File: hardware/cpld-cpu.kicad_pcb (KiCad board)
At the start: 4 copper layers, 264.2 x 190.5 mm, 386 parts, among them J1 Acc, J10 Page, J11 PC_H, J12 Conn_02x16_Odd_Even, J13 Page, J14 Conn_02x16_Odd_Even, J2 X, J3 IR, J4 AXM, J5 Dec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

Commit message: More routing
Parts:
- moved R133 167.5 mm to (281.4, 246.1)
- moved R136 167.5 mm to (281.4, 253.7)
- moved R134 167.5 mm to (281.4, 248.7)
- moved R135 167.5 mm to (281.4, 251.2)
- moved R123 155.6 mm to (281.4, 240.8)
- moved R124 155.6 mm to (281.4, 243.3)
- moved J14 150.6 mm to (266.7, 248.9)
- moved R108 66.0 mm to (190.5, 147.3), turned to 270 degrees
- moved R107 62.7 mm to (188.0, 147.3), turned to 270 degrees
- moved R109 62.5 mm to (185.4, 147.3), turned to 270 degrees
- moved R110 61.4 mm to (182.9, 147.3), turned to 270 degrees
- moved R111 60.6 mm to (180.3, 147.3), turned to 270 degrees
- moved R112 59.9 mm to (177.8, 147.3), turned to 270 degrees
- moved R113 59.5 mm to (175.3, 147.3), turned to 270 degrees
- moved R114 59.3 mm to (172.7, 147.3), turned to 270 degrees
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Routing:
- net /ADDR12: track 0.00 -> 156.2 mm, vias 0 -> 2
- net /IR4: track 17.9 -> 158.7 mm, vias 0 -> 2
- net /ADDR8: track 0.00 -> 134.8 mm, vias 0 -> 3
- net /ADDR9: track 0.00 -> 133.0 mm, vias 0 -> 3
- net /ADDR11: track 0.00 -> 132.8 mm, vias 0 -> 3
- net /ADDR10: track 0.00 -> 132.6 mm, vias 0 -> 3
- net /IR3: track 22.6 -> 151.0 mm, vias 0 -> 2
- net /IR2: track 22.8 -> 148.7 mm, vias 0 -> 2
- net /IR1: track 22.9 -> 145.6 mm, vias 0 -> 2
- net /ADDR0: track 0.00 -> 121.0 mm, vias 0 -> 3
- net /IR0: track 23.1 -> 143.5 mm, vias 0 -> 2
- net /ADDR1: track 0.00 -> 120.0 mm, vias 0 -> 3
- net /ADDR2: track 0.00 -> 118.4 mm, vias 0 -> 3
- net /ADDR6: track 0.00 -> 118.4 mm, vias 0 -> 3
- net /ADDR3: track 0.00 -> 117.0 mm, vias 0 -> 3
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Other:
- board size 264.2 x 190.5 mm -> 264.2 x 193 mm

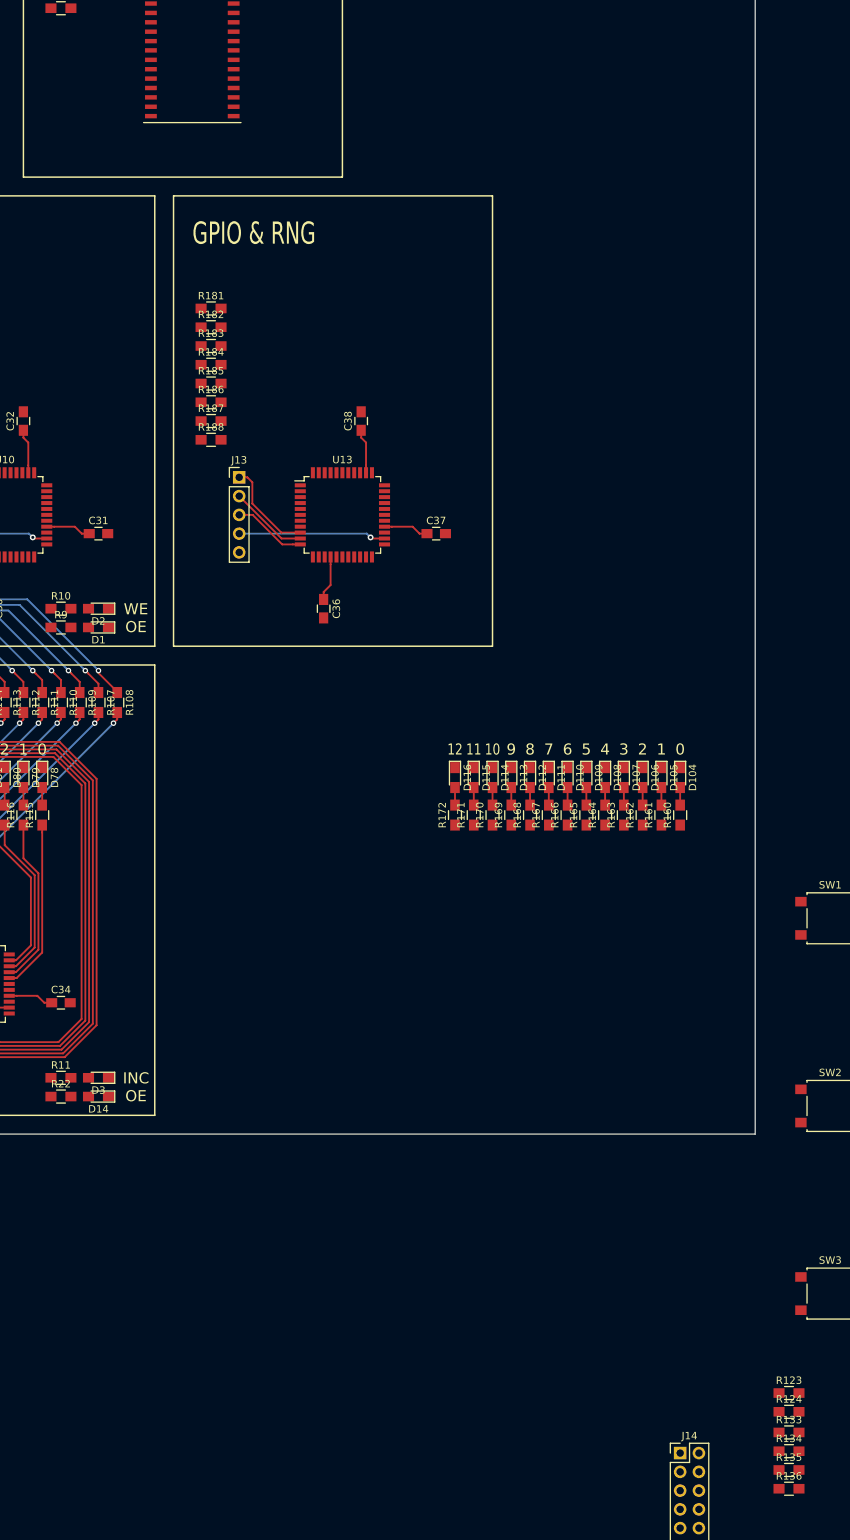
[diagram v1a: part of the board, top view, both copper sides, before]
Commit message: Simplify mem oe/we interface. Makes more pins available on mem_page.
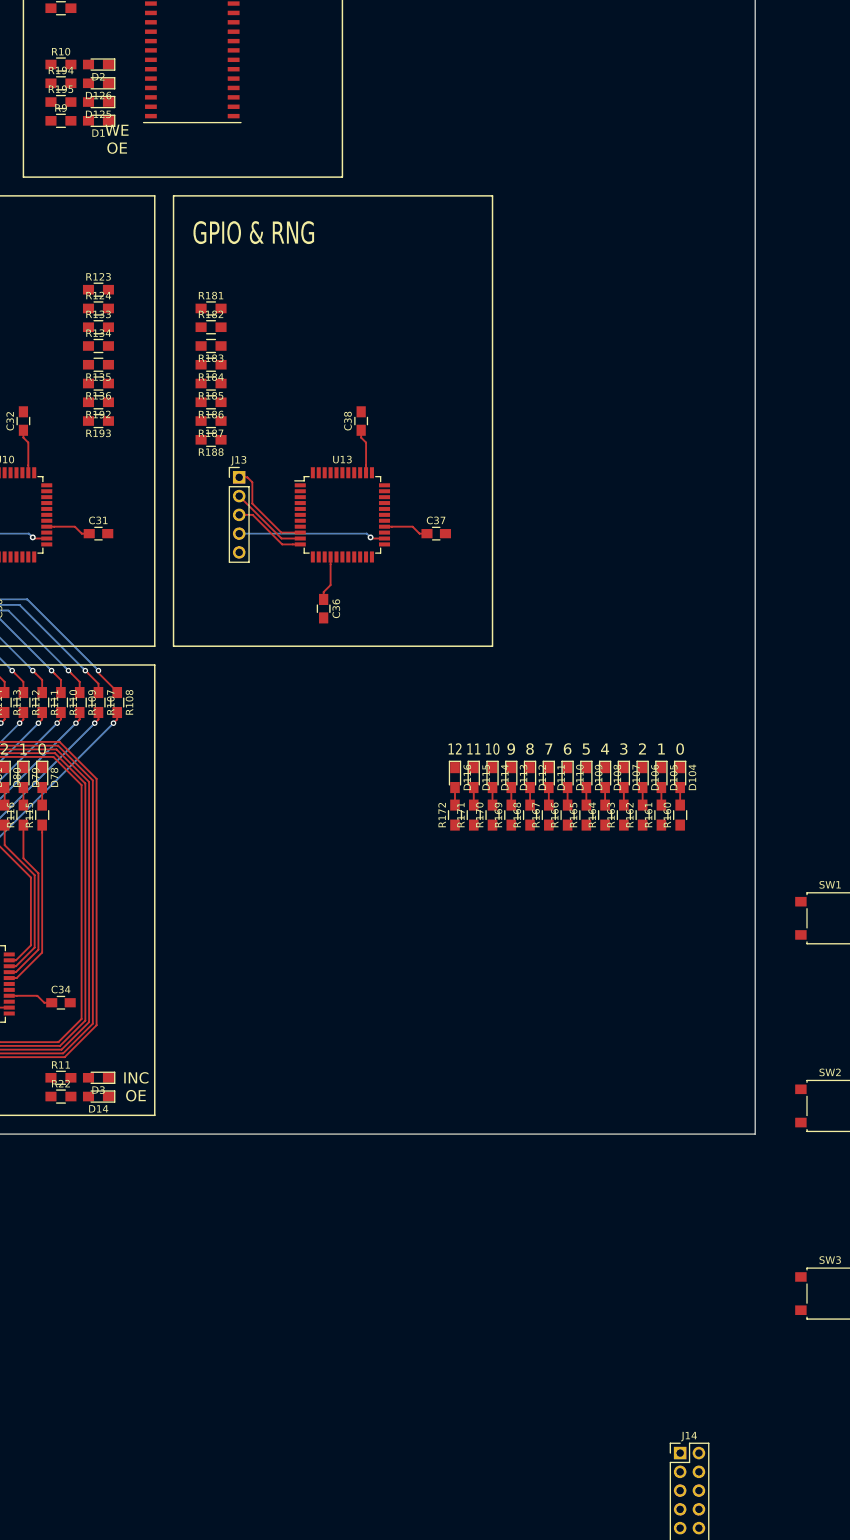
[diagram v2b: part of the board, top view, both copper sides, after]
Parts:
- added D125: LED_Small, LEDs:LED_0805_HandSoldering, F.Cu at (188.0, 66.0)
- added D126: LED_Small, LEDs:LED_0805_HandSoldering, F.Cu at (188.0, 63.5)
- added R192: 470, Resistors_SMD:R_0805_HandSoldering, F.Cu at (188.0, 106.7)
- added R193: 470, Resistors_SMD:R_0805_HandSoldering, F.Cu at (188.0, 109.2)
- added R194: 2k, Resistors_SMD:R_0805_HandSoldering, F.Cu at (182.9, 63.5)
- added R195: 2k, Resistors_SMD:R_0805_HandSoldering, F.Cu at (182.9, 66.0)
- J14: value Conn_02x16_Odd_Even -> Conn_02x17_Odd_Even
- moved R133 176.4 mm to (188.0, 96.5)
- moved R134 176.4 mm to (188.0, 99.1)
- moved R135 176.4 mm to (188.0, 101.6), turned to 180 degrees
- moved R136 176.4 mm to (188.0, 104.1), turned to 180 degrees
- moved R123 176.2 mm to (188.0, 91.4)
- moved R124 176.2 mm to (188.0, 94.0)
- moved D2 73.7 mm to (188.0, 61.0)
- moved R10 73.7 mm to (182.9, 61.0)
- moved D1 68.6 mm to (188.0, 68.6)
- moved R9 68.6 mm to (182.9, 68.6)
- turned R183 to 180 degrees
- turned R184 to 180 degrees
- turned R185 to 180 degrees
- turned R186 to 180 degrees
- turned R187 to 180 degrees
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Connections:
- J14 pad 1: /D0 -> Net-(J14-Pad1)
- J14 pad 10: /ARAM4 -> /ARAM3
- J14 pad 11: /D5 -> /D4
- J14 pad 12: /ARAM5 -> /ARAM4
- J14 pad 13: /D6 -> /D5
- J14 pad 14: /ARAM6 -> /ARAM5
- J14 pad 15: /D7 -> /D6
- J14 pad 16: /ARAM7 -> /ARAM6
- J14 pad 17: /RST -> /D7
- J14 pad 18: /ARAM8 -> /ARAM7
- J14 pad 19: /PAGE0 -> /RST
- J14 pad 2: /ARAM0 -> Net-(J14-Pad2)
- J14 pad 20: /ARAM9 -> /ARAM8
- J14 pad 21: /ARAM14 -> /PAGE0
- J14 pad 22: /ARAM10 -> /ARAM9
- J14 pad 23: /ARAM15 -> /ARAM14
- J14 pad 24: /ARAM11 -> /ARAM10
- J14 pad 25: /ARAM16 -> /ARAM15
- J14 pad 26: /ARAM12 -> /ARAM11
- J14 pad 27: /ARAM17 -> /ARAM16
- J14 pad 28: /ARAM13 -> /ARAM12
- J14 pad 29: Net-(J14-Pad29) -> /ARAM17
- J14 pad 3: /D1 -> /D0
- J14 pad 30: Net-(J14-Pad30) -> /ARAM13
- J14 pad 31: Net-(J14-Pad31) -> /RAM_WE
- J14 pad 32: Net-(J14-Pad32) -> /DEV_OE
- J14 pad 4: /ARAM1 -> /ARAM0
- J14 pad 5: /D2 -> /D1
- J14 pad 6: /ARAM2 -> /ARAM1
- J14 pad 7: /D3 -> /D2
- J14 pad 8: /ARAM3 -> /ARAM2
- J14 pad 9: /D4 -> /D3
- R133 pad 1: /D2 -> Net-(R133-Pad1)
- R133 pad 2: Net-(R133-Pad2) -> /D2
- R134 pad 1: /D3 -> Net-(R134-Pad1)
- R134 pad 2: Net-(R134-Pad2) -> /D3
- R9 pad 1: /RAM_OE -> /GPIO_OE
- U10 pad 1: /ADDR12 -> Net-(U10-Pad1)
- U10 pad 2: Net-(R123-Pad1) -> Net-(U10-Pad2)
- U10 pad 29: /ARAM12 -> /ADDR12
- U10 pad 3: Net-(R124-Pad1) -> Net-(U10-Pad3)
- U10 pad 30: /ARAM13 -> /PAGE0
- U10 pad 31: /ARAM14 -> /ARAM12
- U10 pad 32: /ARAM15 -> /ARAM13
- U10 pad 34: Net-(U10-Pad34) -> /ARAM14
- U10 pad 36: Net-(U10-Pad36) -> /ARAM15
- U10 pad 39: /PAGE0 -> Net-(R123-Pad1)
- U10 pad 40: Net-(U10-Pad40) -> Net-(R124-Pad1)
- U10 pad 41: Net-(U10-Pad41) -> Net-(R133-Pad1)
- U10 pad 42: Net-(U10-Pad42) -> Net-(R134-Pad1)
- U10 pad 44: /RAM_OE -> Net-(U10-Pad44)
- U10 pad 5: Net-(R133-Pad2) -> Net-(R135-Pad2)
- U10 pad 6: Net-(R134-Pad2) -> Net-(R136-Pad2)
- U10 pad 7: Net-(R135-Pad2) -> Net-(R192-Pad2)
- U10 pad 8: Net-(R136-Pad2) -> Net-(R193-Pad2)
- U12 pad 24: Net-(J14-Pad32) -> /RAM_OE
- U12 pad 29: Net-(J14-Pad30) -> /RAM_WE
- U13 pad 34: Net-(J14-Pad29) -> Net-(U13-Pad34)
- U13 pad 36: Net-(J14-Pad31) -> /DEV_OE
- U13 pad 43: Net-(U10-Pad34) -> /RAM_WE
- U13 pad 44: Net-(U10-Pad36) -> /GPIO_OE
- U5 pad 2: /RAM_OE -> /GPIO_OE

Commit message: VHDL for mem_index
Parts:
- J14: footprint Pin_Headers:Pin_Header_Straight_2x16_Pitch2.54mm -> Pin_Headers:Pin_Header_Straight_2x17_Pitch2.54mm
- moved J14 248.9 mm to (147.3, 30.5)
- moved D112 137.5 mm to (124.5, 94.0)
- moved D113 137.5 mm to (121.9, 94.0)
- moved D116 137.5 mm to (114.3, 94.0)
- moved R161 137.5 mm to (142.2, 99.1)
- moved R162 137.5 mm to (139.7, 99.1)
- moved R164 137.5 mm to (134.6, 99.1)
- moved R166 137.5 mm to (129.5, 99.1)
- moved R168 137.5 mm to (124.5, 99.1)
- moved R169 137.5 mm to (121.9, 99.1)
- moved R170 137.5 mm to (119.4, 99.1)
- moved R172 137.5 mm to (114.3, 99.1)
- moved D104 137.5 mm to (144.8, 94.0)
- moved D105 137.5 mm to (142.2, 94.0)
- moved D106 137.5 mm to (139.7, 94.0)
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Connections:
- J14 pad 1: Net-(J14-Pad1) -> /D0
- J14 pad 10: /ARAM3 -> /ARAM4
- J14 pad 11: /D4 -> /D5
- J14 pad 12: /ARAM4 -> /ARAM5
- J14 pad 13: /D5 -> /D6
- J14 pad 14: /ARAM5 -> /ARAM6
- J14 pad 15: /D6 -> /D7
- J14 pad 16: /ARAM6 -> /ARAM7
- J14 pad 17: /D7 -> /RST
- J14 pad 18: /ARAM7 -> /ARAM8
- J14 pad 19: /RST -> /PAGE0
- J14 pad 2: Net-(J14-Pad2) -> /ARAM0
- J14 pad 20: /ARAM8 -> /ARAM9
- J14 pad 21: /PAGE0 -> /ARAM14
- J14 pad 22: /ARAM9 -> /ARAM10
- J14 pad 23: /ARAM14 -> /ARAM15
- J14 pad 24: /ARAM10 -> /ARAM11
- J14 pad 25: /ARAM15 -> /ARAM16
- J14 pad 26: /ARAM11 -> /ARAM12
- J14 pad 27: /ARAM16 -> /ARAM17
- J14 pad 28: /ARAM12 -> /ARAM13
- J14 pad 29: /ARAM17 -> /RAM_WE
- J14 pad 3: /D0 -> /D1
- J14 pad 30: /ARAM13 -> /DEV_OE
- J14 pad 31: /RAM_WE -> /CLK
- J14 pad 32: /DEV_OE -> /RAM_OE
- J14 pad 4: /ARAM0 -> /ARAM1
- J14 pad 5: /D1 -> /D2
- J14 pad 6: /ARAM1 -> /ARAM2
- J14 pad 7: /D2 -> /D3
- J14 pad 8: /ARAM2 -> /ARAM3
- J14 pad 9: /D3 -> /D4
- U5 pad 43: Net-(U5-Pad43) -> /CLK
- U8 pad 20: /X0 -> /ARAM10
- U8 pad 21: /X1 -> /ARAM11
- U8 pad 22: /X2 -> /X0
- U8 pad 23: /X3 -> /X1
- U8 pad 27: /X4 -> /X2
- U8 pad 28: /X5 -> /X3
- U8 pad 29: /X6 -> /X4
- U8 pad 30: /X7 -> /X5
- U8 pad 43: /ARAM10 -> /X6
- U8 pad 44: /ARAM11 -> /X7
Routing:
- net /ARAM0: track 0.00 -> 208.0 mm, vias 0 -> 4
- net /ARAM1: track 0.00 -> 206.5 mm, vias 0 -> 4
- net /ARAM3: track 0.00 -> 205.4 mm, vias 0 -> 5
- net /ARAM7: track 0.00 -> 203.2 mm, vias 0 -> 4
- net /ARAM2: track 0.00 -> 202.2 mm, vias 0 -> 4
- net /ARAM4: track 0.00 -> 202.2 mm, vias 0 -> 4
- net /ARAM6: track 0.00 -> 202.0 mm, vias 0 -> 4
- net /ARAM5: track 0.00 -> 199.8 mm, vias 0 -> 4
- net /ARAM8: track 0.00 -> 195.5 mm, vias 0 -> 4
- net /ARAM9: track 0.00 -> 145.3 mm, vias 0 -> 3
- net /ARAM11: track 0.00 -> 126.6 mm, vias 0 -> 5
- net /ARAM10: track 0.00 -> 125.1 mm, vias 0 -> 5
- net /X4: track 96.6 -> 217.3 mm, vias 2 -> 4
- net /X5: track 101.1 -> 220.7 mm, vias 2 -> 4
- net /X6: track 108.3 -> 206.5 mm, vias 2 -> 4
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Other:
- board text added: "Expn"

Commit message: Route data bus
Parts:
- J12: value Conn_02x16_Odd_Even -> Conn_02x14_Odd_Even; footprint Pin_Headers:Pin_Header_Straight_2x16_Pitch2.54mm -> Pin_Headers:Pin_Header_Straight_2x14_Pitch2.54mm
- SW2: value BTN0 -> BTN1
- SW3: value BTN0 -> BTN2
- moved R180 199.8 mm to (213.4, 99.1), turned to 90 degrees
- moved R179 196.9 mm to (215.9, 99.1), turned to 90 degrees
- moved D124 194.5 mm to (213.4, 94.0), turned to 270 degrees
- moved R178 194.0 mm to (218.4, 99.1), turned to 90 degrees
- moved D123 191.5 mm to (215.9, 94.0), turned to 270 degrees
- moved R177 191.1 mm to (221.0, 99.1), turned to 90 degrees
- moved D122 188.6 mm to (218.4, 94.0), turned to 270 degrees
- moved R176 188.2 mm to (223.5, 99.1), turned to 90 degrees
- moved D121 185.6 mm to (221.0, 94.0), turned to 270 degrees
- moved R175 185.4 mm to (226.1, 99.1), turned to 90 degrees
- moved D120 182.7 mm to (223.5, 94.0), turned to 270 degrees
- moved R174 182.6 mm to (228.6, 99.1), turned to 90 degrees
- moved R173 179.8 mm to (231.1, 99.1), turned to 90 degrees
- moved D119 179.8 mm to (226.1, 94.0), turned to 270 degrees
- moved D118 176.9 mm to (228.6, 94.0), turned to 270 degrees
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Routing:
- net /D6: track 0.00 -> 443.7 mm, vias 0 -> 10
- net /D7: track 0.00 -> 435.8 mm, vias 0 -> 10
- net /D5: track 0.00 -> 426.1 mm, vias 0 -> 10
- net /D2: track 0.00 -> 416.7 mm, vias 0 -> 10
- net /D3: track 0.00 -> 415.0 mm, vias 0 -> 10
- net /D1: track 0.00 -> 409.2 mm, vias 0 -> 12
- net /D0: track 0.00 -> 405.5 mm, vias 0 -> 10
- net /D4: track 0.00 -> 370.6 mm, vias 0 -> 9
- net /ARAM15: track 0.00 -> 146.0 mm, vias 0 -> 3
- net /ARAM13: track 0.00 -> 141.3 mm, vias 0 -> 4
- net /ARAM12: track 0.00 -> 129.9 mm, vias 0 -> 4
- net /ARAM14: track 0.00 -> 126.0 mm, vias 0 -> 3
- net /ARAM17: track 0.00 -> 125.5 mm, vias 0 -> 2
- net /ARAM16: track 0.00 -> 120.3 mm, vias 0 -> 4
- net /PAGE0: track 46.4 -> 139.0 mm, vias 2 -> 3
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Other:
- outline, holes or cut-outs redrawn
- board text added: "(AR)"
- board text added: "(IR)"
- board text added: "(PC)"
- board text added: "Address"
- board text added: "Instruction"
- board text added: "Program Counter"
- board text removed: "Address (AR)"
- board text removed: "Instruction (IR)"
- board text removed: "Program Counter (PC)"

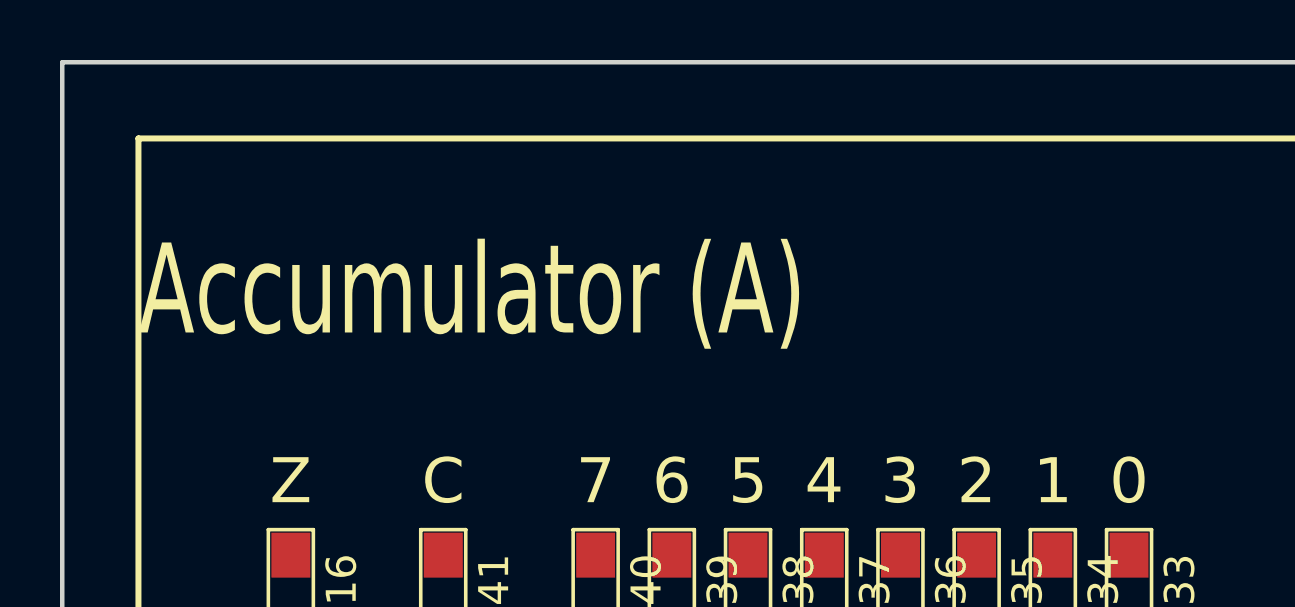
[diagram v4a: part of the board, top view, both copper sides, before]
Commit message: Clock schematic
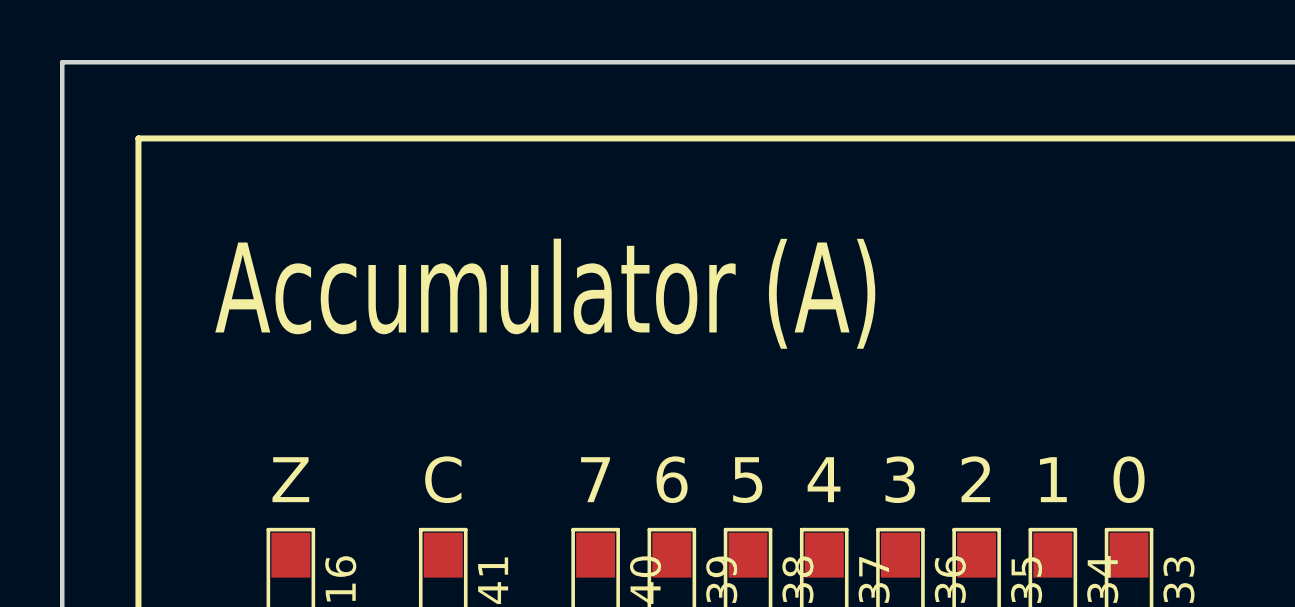
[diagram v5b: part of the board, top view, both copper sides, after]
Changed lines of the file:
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@@
   (gr_line (start 60.96 78.74) (end 15.24 78.74) (layer F.SilkS) (width 0.2))
   (gr_line (start 15.24 78.74) (end 15.24 139.7) (layer F.SilkS) (width 0.2))
-  (gr_text "Accumulator (A)" (at 15.24 20.32) (layer F.SilkS)
+  (gr_text "Accumulator (A)" (at 17.78 20.32) (layer F.SilkS)
     (effects (font (size 3 2) (thickness 0.3)) (justify left))
   )
